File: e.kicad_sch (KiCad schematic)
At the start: 9 parts, among them SW1 SW_Push, SW2 SW_Push, U2 MAX98357A

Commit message: i did a thing
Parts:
- added D2: D_Schottky, Diode_SMD:D_SOD-323, symbol Device:D_Schottky
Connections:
- net VCC is gone; now on net +3V0: R1.1
- net +3V0: now also D2.2 (A); no longer A1.39 (VSYS)
- net GND: now also U1.3 (GND), U2.6 (NC); no longer U1.2 (GND), U2.17 (PAD), U2.3 (GND)
- net at LS1.1: now also U2.8 (OUTP); no longer U2.9 (OUTP)
- net at LS1.2: now also U2.9 (OUTN); no longer U2.10 (OUTN)
- net at A1.1 (GPIO0): now also U2.3 (DIN); no longer U2.1 (DIN)
- net at A1.2 (GPIO1): now also U2.2 (BCLK); no longer U2.16 (BCLK)
- net at A1.4 (GPIO2): now also U2.1 (LRCLK); no longer U2.14 (LRCLK)
- net at R2.1: now also U2.4 (GAIN_SLOT); no longer U2.2 (GAIN_SLOT)
- new net: A1.39 (VSYS), D2.1 (K)
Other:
- note added: "THIS IS THE 1.54" VERSION BTW <<<<<<<<<<<<<<<<<<<"
- note removed: "THIS IS THE 1.3" VERSION BTW <<<<<<<<<<<<<<<<<<<"

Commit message: i did MORE things
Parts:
- SW1: value SW_Push -> pwr
- SW2: value SW_Push -> rst
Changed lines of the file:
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@@
 			)
 		)
-		(property "Value" "SW_Push"
+		(property "Value" "rst"
 			(at 134.62 167.6399 90)
 			(show_name no)
@@
 			)
 		)
-		(property "Value" "SW_Push"
+		(property "Value" "pwr"
 			(at 199.39 67.3099 90)
 			(show_name no)

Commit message: its all doom and despair from here on out
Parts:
- LS1: footprint (none) -> stupid-dumb-speaker:stupid-dumb-speaker
- SW1: value pwr -> usr
- U1: footprint (none) -> display-lol:display-lol
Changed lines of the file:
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@@
 			)
 		)
-		(property "Footprint" ""
+		(property "Footprint" "stupid-dumb-speaker:stupid-dumb-speaker"
 			(at 83.82 115.57 0)
 			(hide yes)
@@
 			)
 		)
-		(property "Footprint" ""
+		(property "Footprint" "display-lol:display-lol"
 			(at 165.1 106.68 0)
 			(hide yes)
@@
 			)
 		)
-		(property "Datasheet" "https://www.waveshare.com/w/upload/a/ae/ST7789_Datasheet.pdf"
+		(property "Datasheet" "https://cdn-shop.adafruit.com/product-files/3787/3787_tft_QT154H2201__________20190228182902.pdf"
 			(at 165.1 106.68 0)
 			(hide yes)
@@
 			)
 		)
-		(property "Value" "pwr"
+		(property "Value" "usr"
 			(at 199.39 67.3099 90)
 			(show_name no)

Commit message: i rembered to put the ground plane this time trust
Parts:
- SW1, SW2: footprint Button_Switch_SMD:SW_SPST_B3U-3100P-B -> Button_Switch_SMD:SW_SPST_B3S-1000
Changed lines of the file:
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@@
 			)
 		)
-		(property "Footprint" "Button_Switch_SMD:SW_SPST_B3U-3100P-B"
+		(property "Footprint" "Button_Switch_SMD:SW_SPST_B3S-1000"
 			(at 128.27 166.37 0)
 			(hide yes)
@@
 			)
 		)
-		(property "Footprint" "Button_Switch_SMD:SW_SPST_B3U-3100P-B"
+		(property "Footprint" "Button_Switch_SMD:SW_SPST_B3S-1000"
 			(at 200.66 66.04 0)
 			(hide yes)

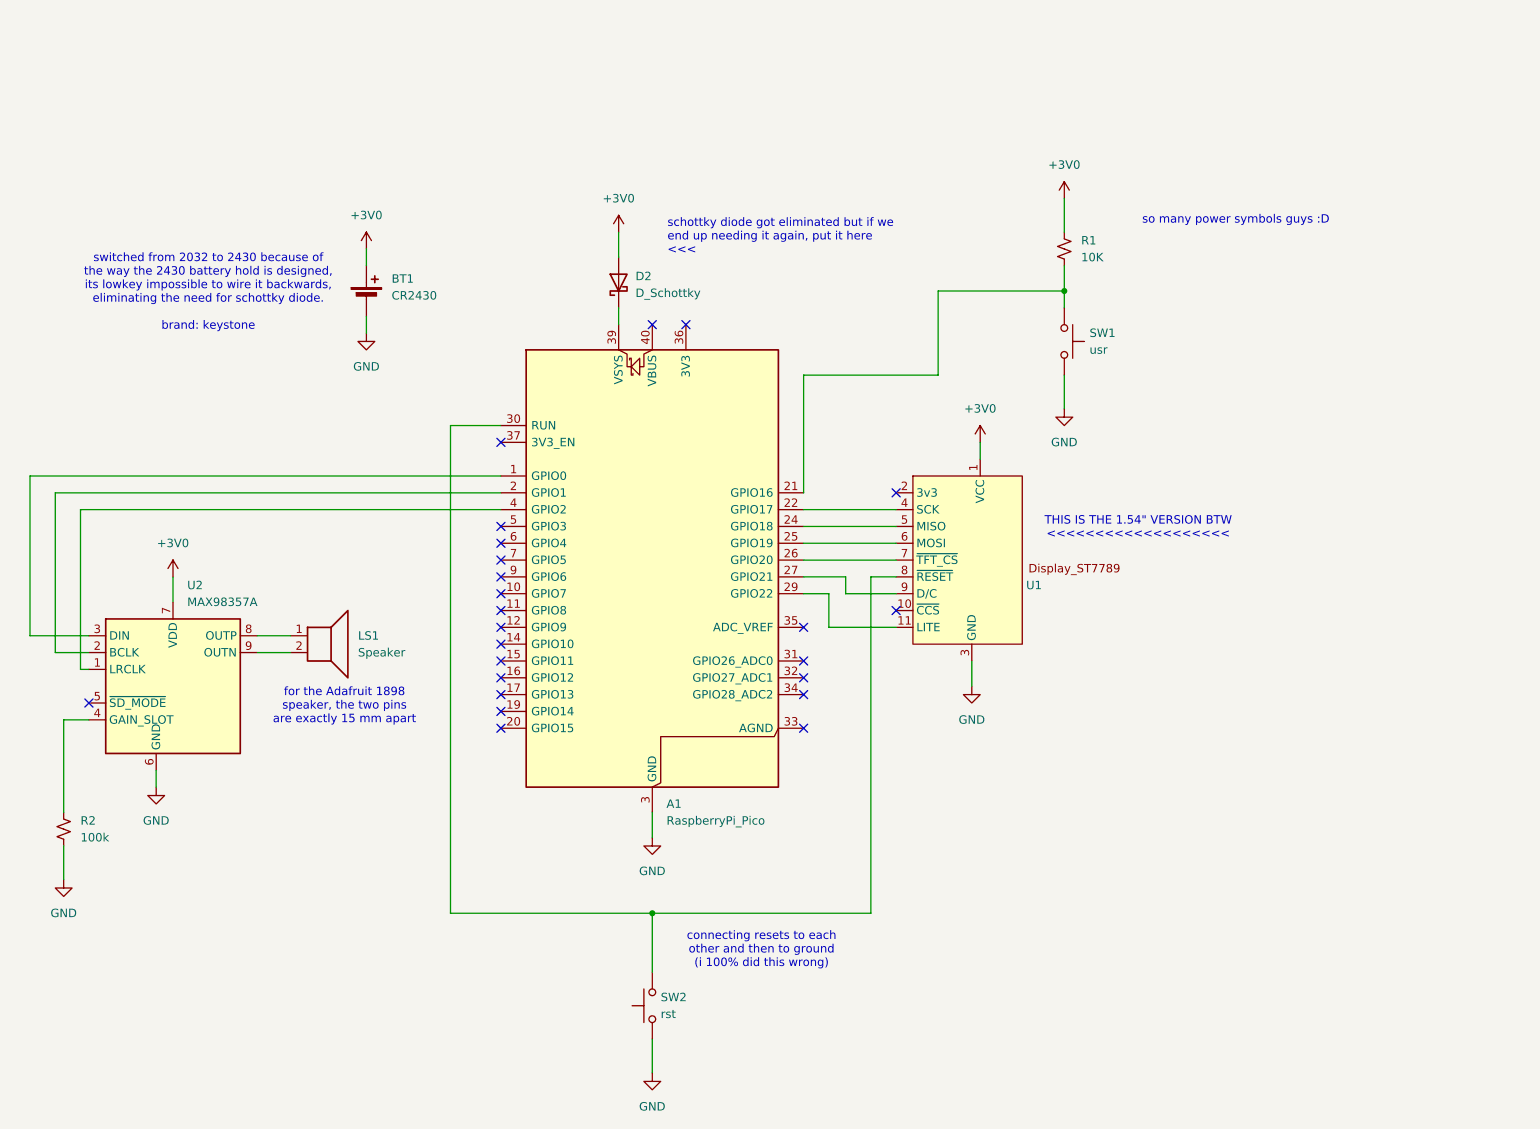
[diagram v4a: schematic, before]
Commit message: the board is smaller (but is it cheaper...?)
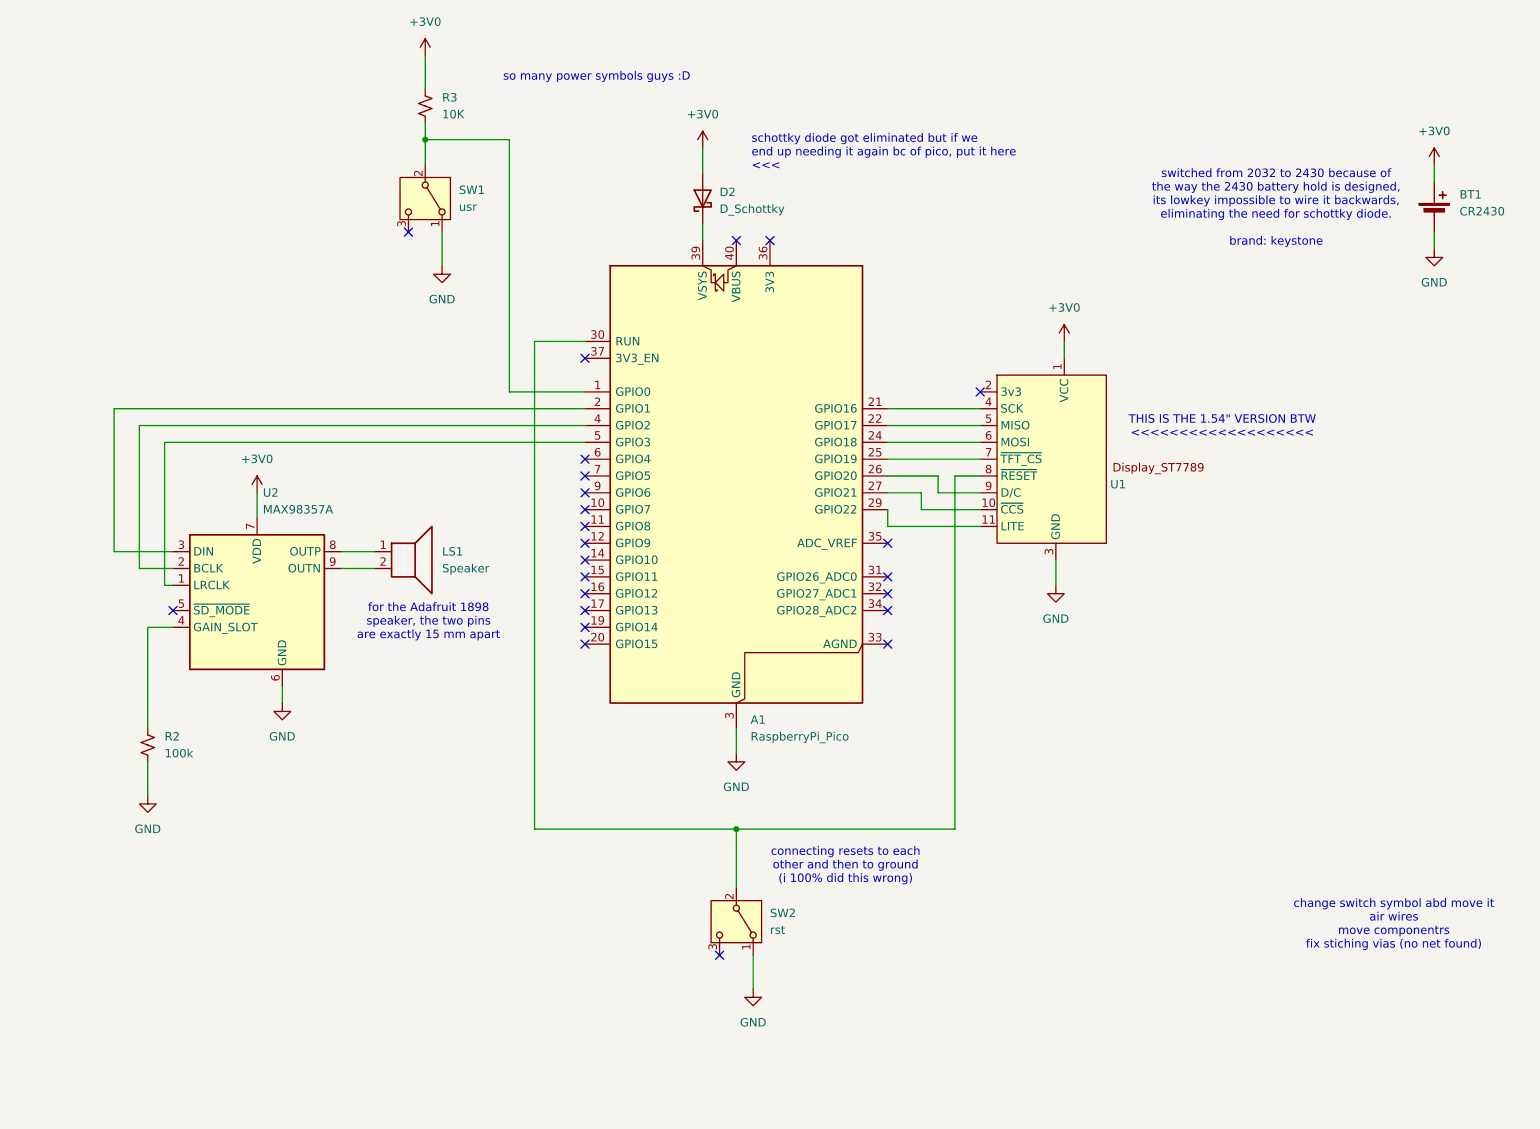
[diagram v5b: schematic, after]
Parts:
- removed R1: 10K, Resistor_SMD:R_1206_3216Metric, symbol Device:R_Small_US
- removed SW1: usr, Button_Switch_SMD:SW_SPST_B3S-1000, symbol Switch:SW_Push
- removed SW2: rst, Button_Switch_SMD:SW_SPST_B3S-1000, symbol Switch:SW_Push
- added R3: 10K, Resistor_SMD:R_1206_3216Metric, symbol Device:R_Small_US
- added SW1: usr, Button_Switch_THT:SW_Slide_SPDT_Straight_CK_OS102011MS2Q, symbol Switch:SW_SPDT
- added SW2: rst, Button_Switch_THT:SW_Slide_SPDT_Straight_CK_OS102011MS2Q, symbol Switch:SW_SPDT
- LS1: footprint stupid-dumb-speaker:stupid-dumb-speaker -> custom-fp:stupid-dumb-speaker
- U1: footprint display-lol:display-lol -> custom-fp:display-lol
- U2: footprint Package_DFN_QFN:TQFN-16-1EP_3x3mm_P0.5mm_EP1.23x1.23mm -> custom-fp:MAX98357A
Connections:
- net +3V0: now also R3.1; no longer U2.8 (OUTP)
- net GND: now also SW1.1 (A), SW2.1 (A); no longer U2.11 (GND), U2.15 (GND)
- net at A1.1 (GPIO0): now also R3.2, SW1.2 (B); no longer U2.3 (DIN)
- net at A1.2 (GPIO1): now also U2.3 (DIN); no longer U2.2 (BCLK)
- net at A1.21 (GPIO16): now also U1.4 (SCK)
- net at A1.22 (GPIO17): now also U1.5 (MISO); no longer U1.4 (SCK)
- net at A1.24 (GPIO18): now also U1.6 (MOSI); no longer U1.5 (MISO)
- net at A1.25 (GPIO19): now also U1.7 (~{TFT_CS}); no longer U1.6 (MOSI)
- net at A1.26 (GPIO20): now also U1.9 (D/C); no longer U1.7 (~{TFT_CS})
- net at A1.27 (GPIO21): now also U1.10 (~{CCS}); no longer U1.9 (D/C)
- net at A1.30 (RUN), U1.8 (~{RESET}): now also SW2.2 (B)
- net at A1.4 (GPIO2): now also U2.2 (BCLK); no longer U2.1 (LRCLK)
- net at A1.5 (GPIO3): now also U2.1 (LRCLK)
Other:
- note added: "change switch symbol abd move it air wires move componentrs fix stiching vias (no net found)"
- note added: "schottky diode got eliminated but if we end up needing it again bc of pico, put it here <<<"
- note removed: "schottky diode got eliminated but if we end up needing it again, put it here <<<"
- moved on the sheet: A1, BT1, D2, LS1, R2, U1, U2

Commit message: the board is smaller... and cooler... and slightly cheaper!!
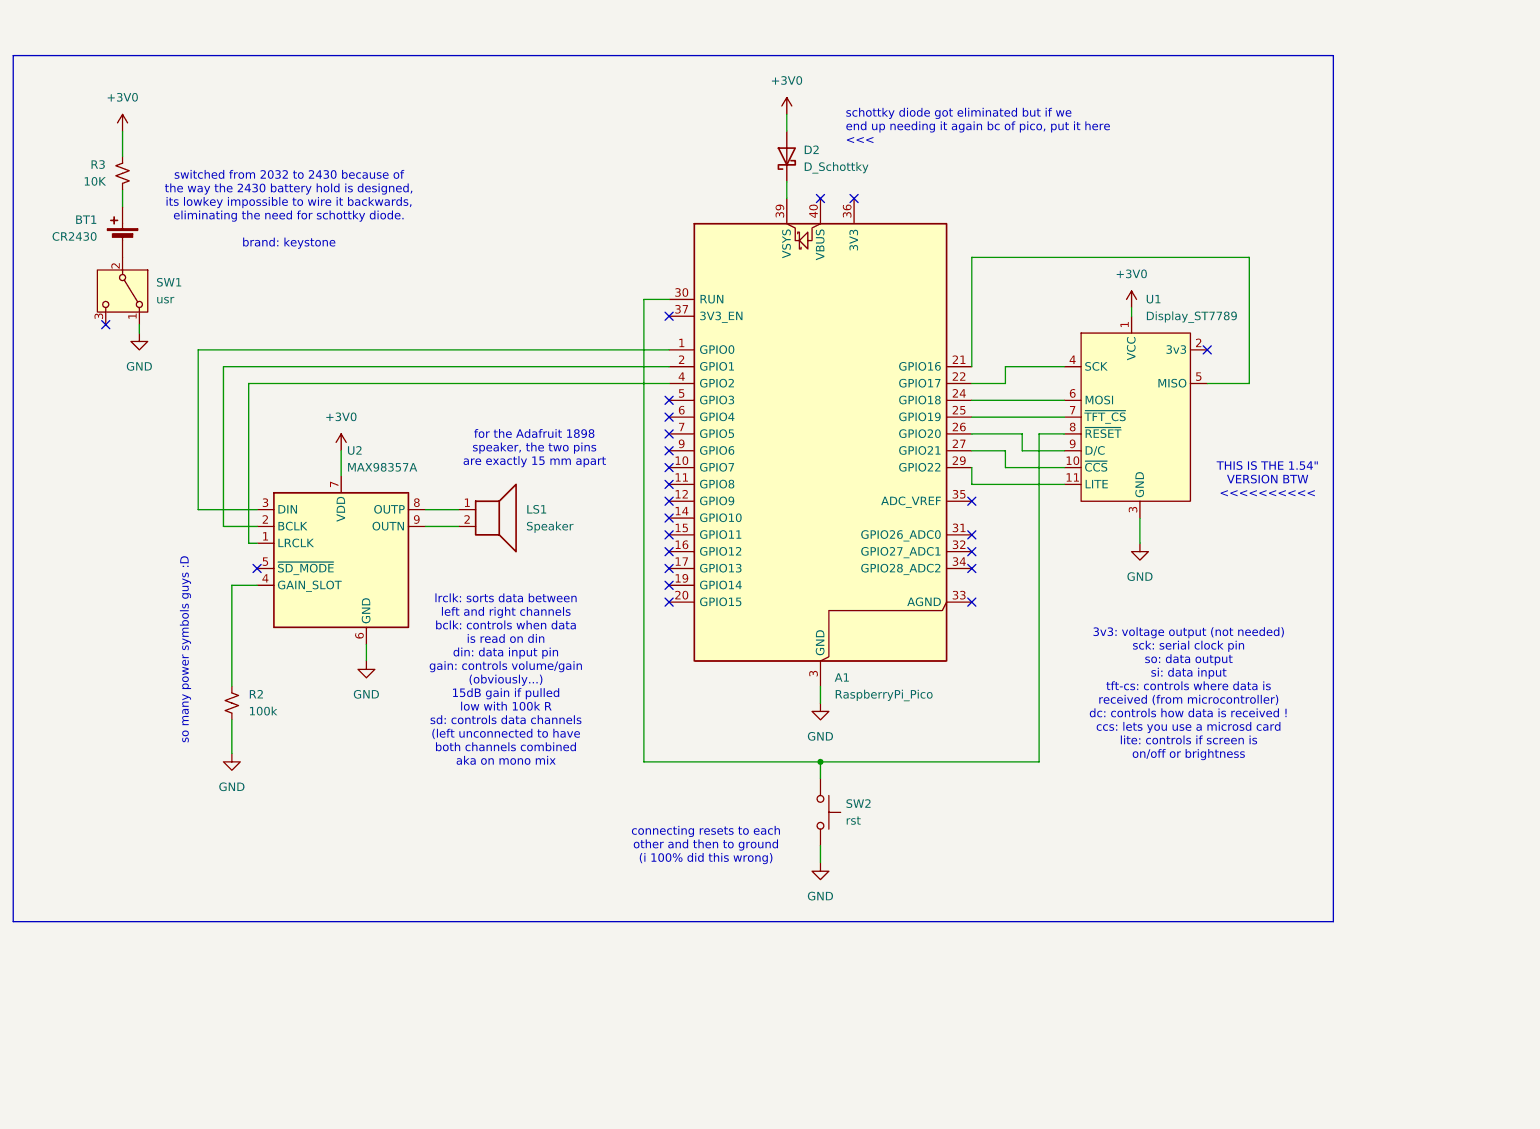
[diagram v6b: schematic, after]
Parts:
- removed SW2: rst, Button_Switch_THT:SW_Slide_SPDT_Straight_CK_OS102011MS2Q, symbol Switch:SW_SPDT
- removed U1: (no value), custom-fp:display-lol, symbol display_idk_lol:small-display
- added SW2: rst, Button_Switch_SMD:SW_Push_1P1T_NO_CK_KMR2, symbol Switch:SW_Push
- added U1: Display_ST7789, custom-fp:display-lol, symbol cool-stuff:small-display
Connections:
- net +3V0: now also U1.1 (VCC); no longer BT1.1 (+)
- net GND: now also SW2.2, U1.3 (GND); no longer BT1.2 (-)
- net at U2.3 (DIN): now also A1.1 (GPIO0); no longer A1.2 (GPIO1)
- net at A1.21 (GPIO16): now also U1.5 (MISO)
- net at A1.22 (GPIO17): now also U1.4 (SCK)
- net at A1.24 (GPIO18): now also U1.6 (MOSI)
- net at A1.25 (GPIO19): now also U1.7 (~{TFT_CS})
- net at A1.26 (GPIO20): now also U1.9 (D/C)
- net at A1.27 (GPIO21): now also U1.10 (~{CCS})
- net at A1.29 (GPIO22): now also U1.11 (LITE)
- net at A1.30 (RUN): now also SW2.1, U1.8 (~{RESET})
- net at U2.2 (BCLK): now also A1.2 (GPIO1); no longer A1.4 (GPIO2)
- net at U2.1 (LRCLK): now also A1.4 (GPIO2); no longer A1.5 (GPIO3)
- new net: BT1.2 (-), SW1.2 (B)
- new net: BT1.1 (+), R3.2
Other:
- note added: "3v3: voltage output (not needed) sck: serial clock pin so: data output si: data input tft-cs: controls where data is received (from microcontroller) dc: controls how data is received ! ccs: lets you use a microsd card lite: controls if screen is on/off or brightness"
- note added: "THIS IS THE 1.54" VERSION BTW <<<<<<<<<<"
- note added: "lrclk: sorts data between left and right channels bclk: controls when data is read on din din: data input pin gain: controls volume/gain (obviously...) 15dB gain if pulled low with 100k R sd: controls data channels (left unconnected to have both channels combined aka on mono mix"
- note removed: "THIS IS THE 1.54" VERSION BTW <<<<<<<<<<<<<<<<<<<"
- note removed: "change switch symbol abd move it air wires move componentrs fix stiching vias (no net found)"
- moved on the sheet: A1, BT1, D2, LS1, R2, U2
